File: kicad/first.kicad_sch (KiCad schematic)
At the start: 84 parts, among them J1 Conn_01x04_Pin, P1 USB_C_Plug_USB2.0, Q1 MMUN2111LT1G, Q2 MMBT3904, SW1 SW_SPDT, U1 STM32F407VETx, U2 LP5907MFX-3.3, U3 CS4272, U4 NE5532, U5 NE5532, U6 NE5532, U7 NE5532, Y1 X MHz

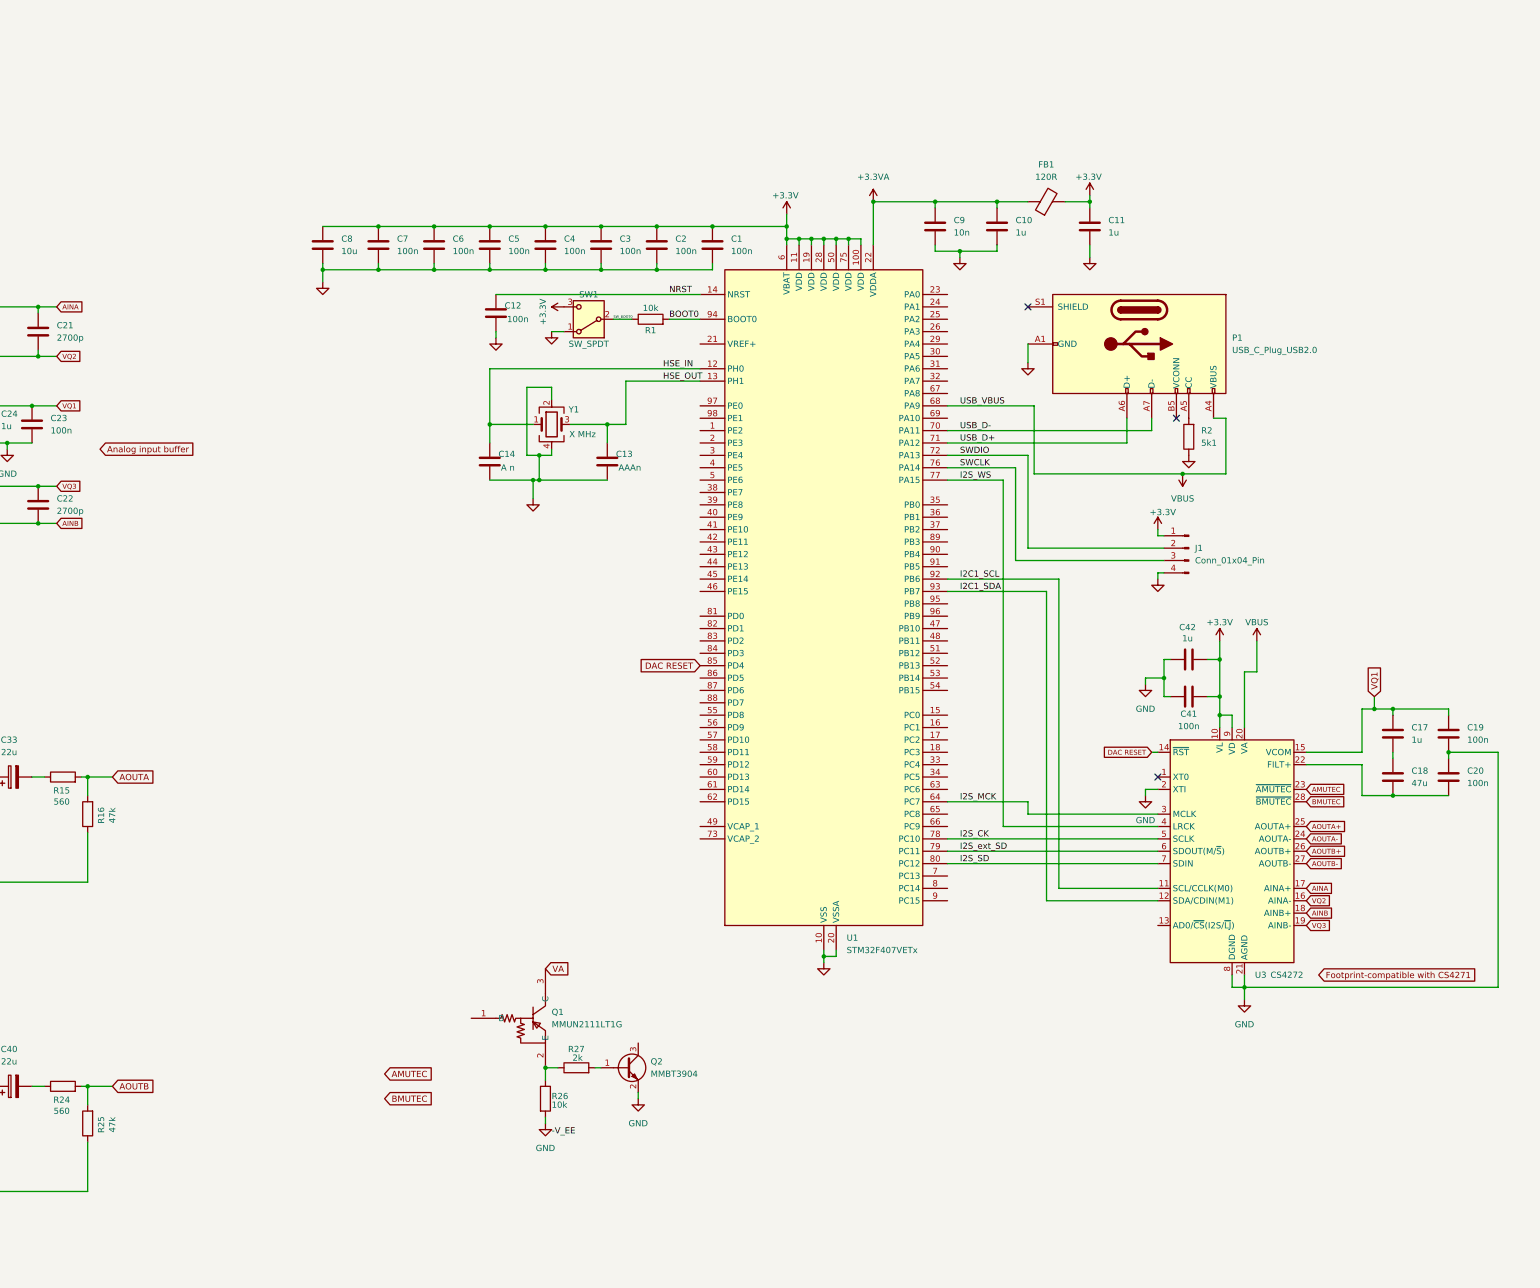
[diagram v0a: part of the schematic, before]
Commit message: codec analog supply filter, added mute control circuits
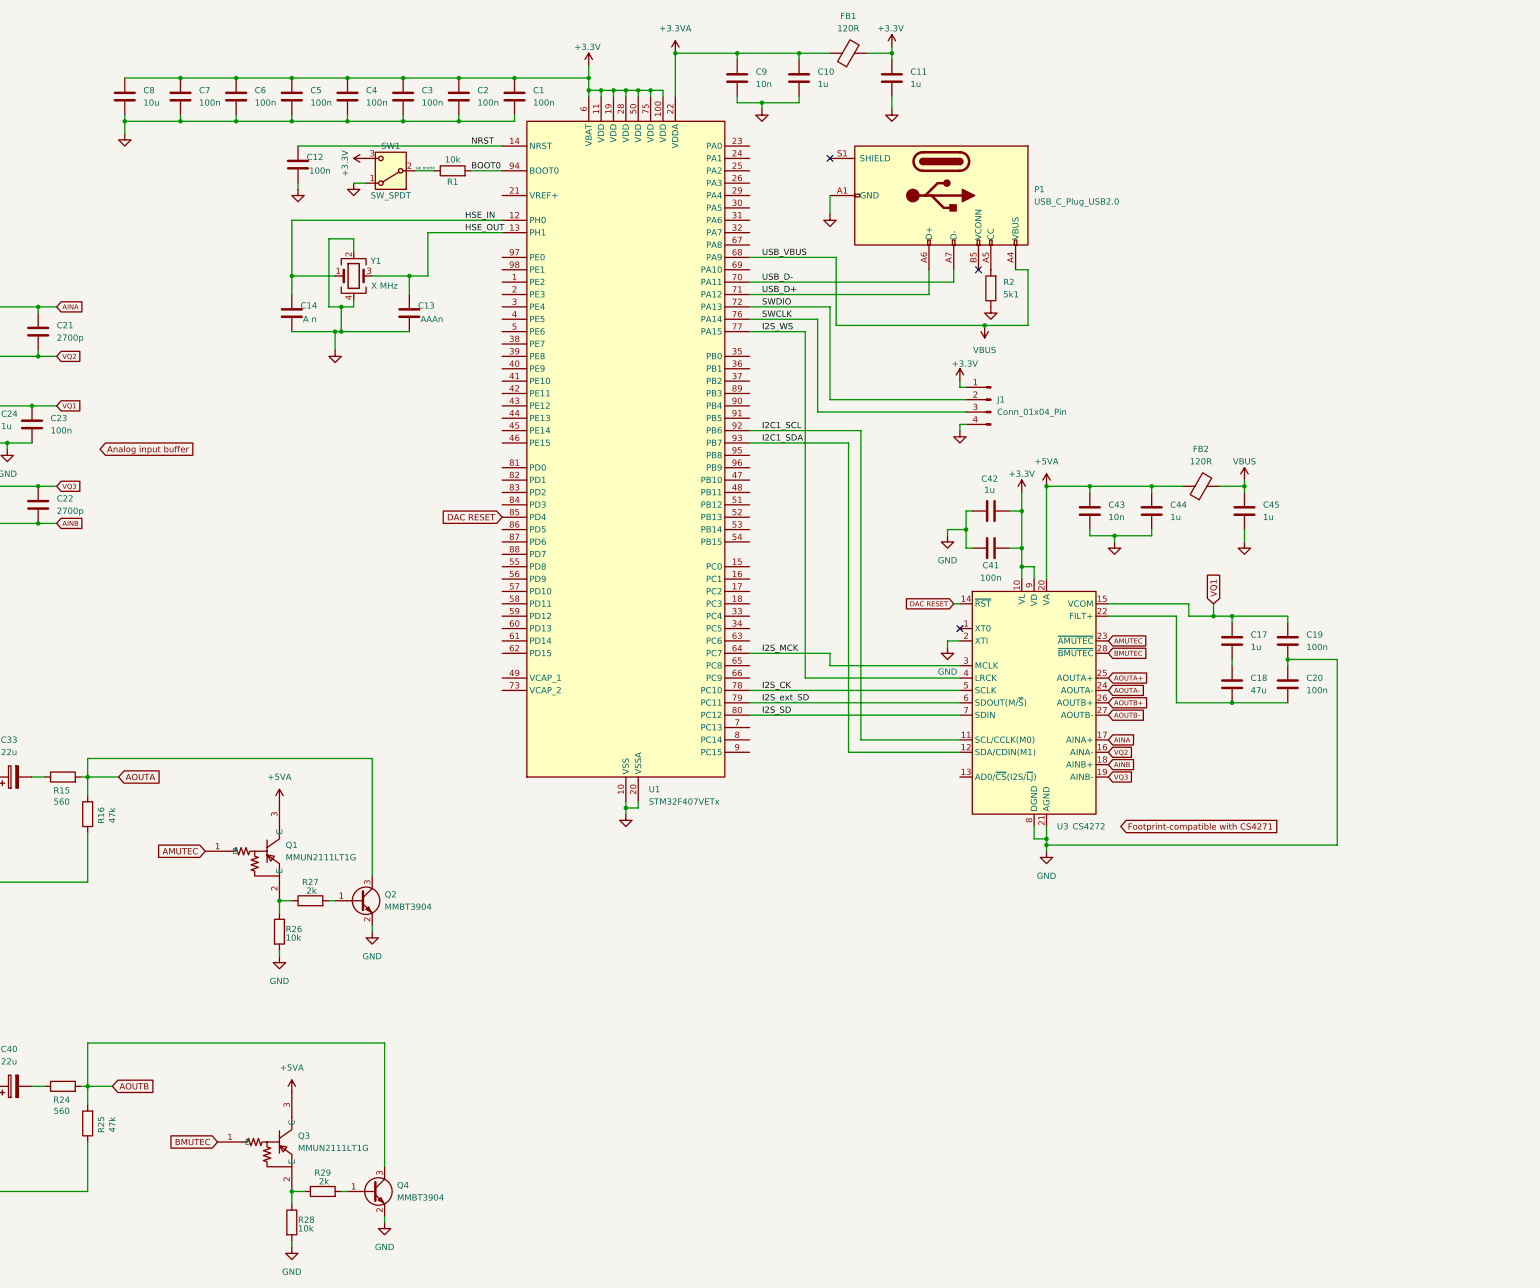
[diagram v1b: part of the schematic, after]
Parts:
- added C43: 10n, symbol Device:C
- added C44, C45: 1u, symbol Device:C
- added FB2: 120R, symbol Device:FerriteBead
- added Q3: MMUN2111LT1G, easyeda2kicad:SOT-23-3_L2.9-W1.3-P1.90-LS2.4-BR, symbol easyeda2kicad:MMUN2111LT1G
- added Q4: MMBT3904, Package_TO_SOT_SMD:SOT-23, symbol Transistor_BJT:MMBT3904
- added R28: 10k, symbol Device:R
- added R29: 2k, symbol Device:R
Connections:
- net AMUTEC: now also Q1.1 (B)
- net AOUTA: now also Q2.3 (C)
- net AOUTB: now also Q4.3 (C)
- net BMUTEC: now also Q3.1 (B)
- net GND: now also C43.2, C44.2, C45.2, Q4.2 (E), R28.2
- net VBUS: now also C45.1, FB2.2; no longer U3.20 (VA)
- net VA renamed +5VA
- net +5VA: now also U3.20 (VA), C43.1, C44.1, FB2.1, Q3.3 (C)
- new net: Q3.2 (E), R28.1, R29.1
- new net: Q4.1 (B), R29.2
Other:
- moved on the sheet: C1, C10, C11, C12, C13, C14, C17, C18, C19, C2, C20, C3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

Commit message: descriptive text
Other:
- note added: "Analog input buffer"
- note added: "Analog output filters"
- note added: "Debug connector"
- note added: "Footprint compatible with CS4271"
- note added: "Mute circuits"
- moved on the sheet: C15, C16, D1, R3, U2

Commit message: rotary encoders
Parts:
- added SW2, SW3, SW4: RotaryEncoder_Switch_MP, symbol Device:RotaryEncoder_Switch_MP
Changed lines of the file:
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@@
 	)
 	(symbol
+		(lib_id "Device:RotaryEncoder_Switch_MP")
+		(at 275.59 214.63 0)
+		(unit 1)
+		(exclude_from_sim no)
+		(in_bom yes)
+		(on_board yes)
+		(dnp no)
+		(fields_autoplaced yes)
+		(property "Reference" "SW3"
+			(at 275.59 204.47 0)
+			(effects
+				(font
+					(size 1.27 1.27)
+				)
+			)
+		)
+		(property "Value" "RotaryEncoder_Switch_MP"
+			(at 275.59 207.01 0)
+			(effects
+				(font
+					(size 1.27 1.27)
+				)
+			)
+		)
+		(property "Footprint" ""
+			(at 271.78 210.566 0)
+			(effects
+				(font
+					(size 1.27 1.27)
+				)
+				(hide yes)
+			)
+		)
+		(property "Datasheet" "~"
+			(at 275.59 227.33 0)
+			(effects
+				(font
+					(size 1.27 1.27)
+				)
+				(hide yes)
+			)
+		)
+		(property "Description" "Rotary encoder, dual channel, incremental quadrate outputs, with switch and MP Pin"
+			(at 275.59 229.87 0)
+			(effects
+				(font
+					(size 1.27 1.27)
+				)
+				(hide yes)
+			)
+		)
+		(pin "A"
+		)
+		(pin "MP"
+		)
+		(pin "S1"
+		)
+		(pin "C"
+		)
+		(pin "B"
+		)
+		(pin "S2"
+		)
+		(instances
+			(project "first"
+				(path "/580becc7-fa47-4b4d-a43e-4b9316967eb7"
+					(reference "SW3")
+					(unit 1)
+				)
+			)
+		)
+	)
+	(symbol
 		(lib_id "Device:R")
 		(at 373.38 35.56 0)
@@
 	)
 	(symbol
+		(lib_id "Device:RotaryEncoder_Switch_MP")
+		(at 246.38 214.63 0)
+		(unit 1)
+		(exclude_from_sim no)
+		(in_bom yes)
+		(on_board yes)
+		(dnp no)
+		(fields_autoplaced yes)
+		(property "Reference" "SW2"
+			(at 246.38 204.47 0)
+			(effects
+				(font
+					(size 1.27 1.27)
+				)
+			)
+		)
+		(property "Value" "RotaryEncoder_Switch_MP"
+			(at 246.38 207.01 0)
+			(effects
+				(font
+					(size 1.27 1.27)
+				)
+			)
+		)
+		(property "Footprint" ""
+			(at 242.57 210.566 0)
+			(effects
+				(font
+					(size 1.27 1.27)
+				)
+				(hide yes)
+			)
+		)
+		(property "Datasheet" "~"
+			(at 246.38 227.33 0)
+			(effects
+				(font
+					(size 1.27 1.27)
+				)
+				(hide yes)
+			)
+		)
+		(property "Description" "Rotary encoder, dual channel, incremental quadrate outputs, with switch and MP Pin"
+			(at 246.38 229.87 0)
+			(effects
+				(font
+					(size 1.27 1.27)
+				)
+				(hide yes)
+			)
+		)
+		(pin "A"
+		)
+		(pin "MP"
+		)
+		(pin "S1"
+		)
+		(pin "C"
+		)
+		(pin "B"
+		)
+		(pin "S2"
+		)
+		(instances
+			(project ""
+				(path "/580becc7-fa47-4b4d-a43e-4b9316967eb7"
+					(reference "SW2")
+					(unit 1)
+				)
+			)
+		)
+	)
+	(symbol
 		(lib_id "Audio:CS4272")
 		(at 311.15 161.29 0)
@@
 					(unit 1)
 				)
+			)
+		)
+	)
+	(symbol
+		(lib_id "Device:RotaryEncoder_Switch_MP")
+		(at 259.08 240.03 0)
+		(unit 1)
+		(exclude_from_sim no)
+		(in_bom yes)
+		(on_board yes)
+		(dnp no)
+		(fields_autoplaced yes)
+		(property "Reference" "SW4"
+			(at 259.08 229.87 0)
+			(effects
+				(font
+					(size 1.27 1.27)
+				)
+			)
+		)
+		(property "Value" "RotaryEncoder_Switch_MP"
+			(at 259.08 232.41 0)
+			(effects
+				(font
+					(size 1.27 1.27)
+				)
+			)
+		)
+		(property "Footprint" ""
+			(at 255.27 235.966 0)
+			(effects
+				(font
+					(size 1.27 1.27)
+				)
+				(hide yes)
+			)
+		)
+		(property "Datasheet" "~"
+			(at 259.08 252.73 0)
+			(effects
+				(font
+					(size 1.27 1.27)
+				)
+				(hide yes)
+			)
+		)
+		(property "Description" "Rotary encoder, dual channel, incremental quadrate outputs, with switch and MP Pin"
+			(at 259.08 255.27 0)
+			(effects
+				(font
+					(size 1.27 1.27)
+				)
+				(hide yes)
+			)
+		)
+		(pin "A"
+		)
+		(pin "MP"
+		)
+		(pin "S1"
+		)
+		(pin "C"
+		)
+		(pin "B"
+		)
+		(pin "S2"
+		)
+		(instances
+			(project "first"
+				(path "/580becc7-fa47-4b4d-a43e-4b9316967eb7"
+					(reference "SW4")
+					(unit 1)
+				)

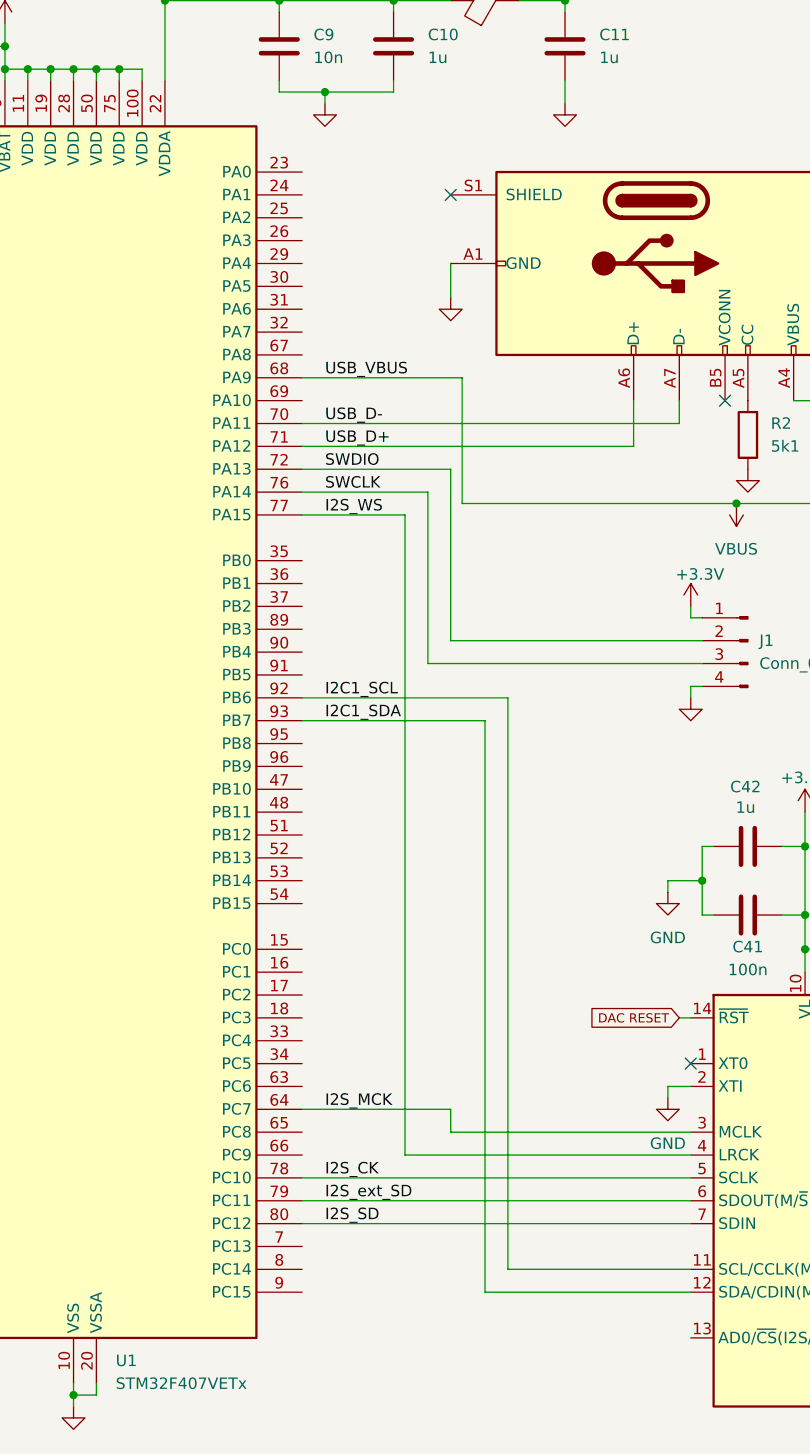
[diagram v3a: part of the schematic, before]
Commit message: assigned timer pins, moved I2C clk and data
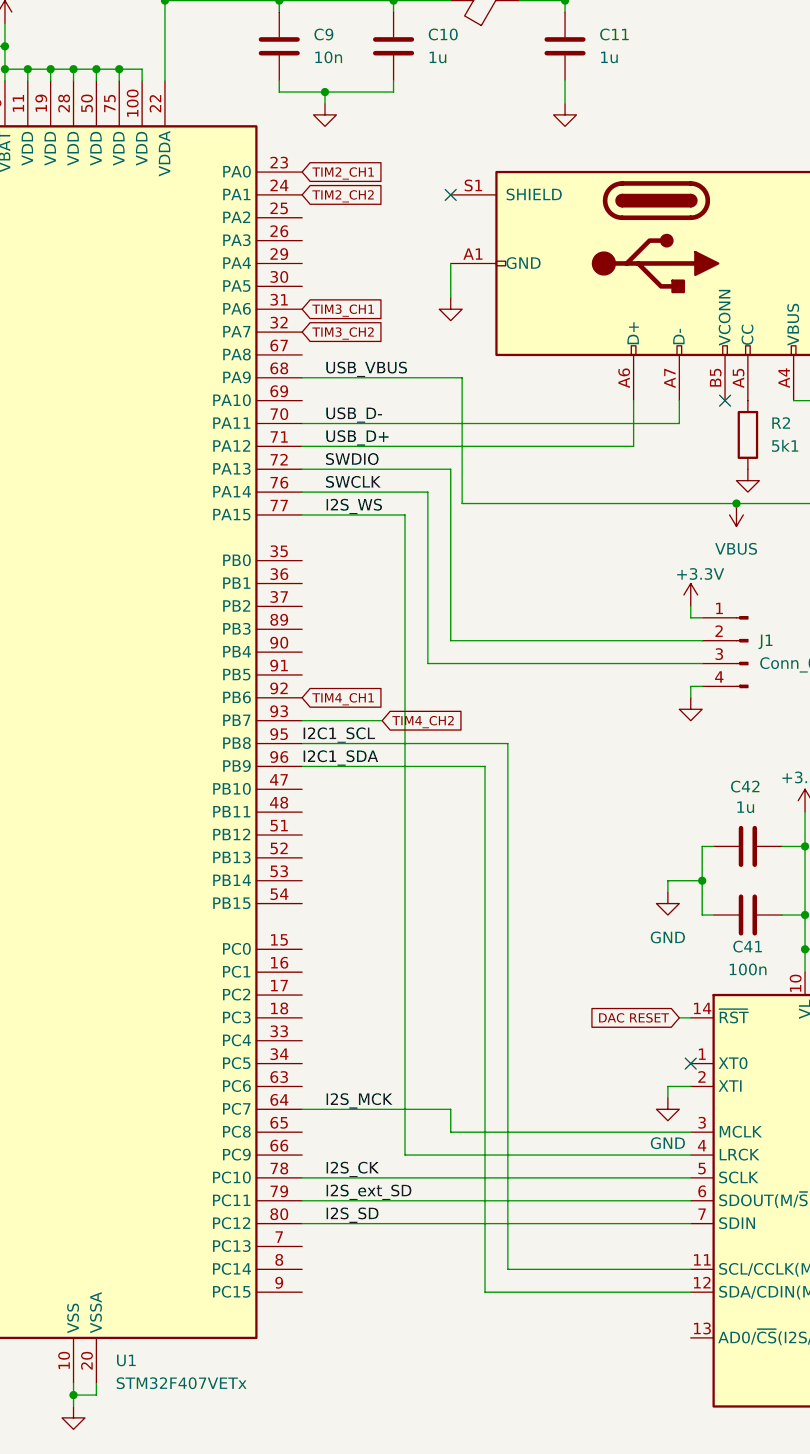
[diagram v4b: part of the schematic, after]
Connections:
- net I2C1_SCL: now also U1.95 (PB8); no longer U1.92 (PB6)
- net I2C1_SDA: now also U1.96 (PB9); no longer U1.93 (PB7)
- net TIM2_CH1: now reaches U1.23 (PA0)
- net TIM2_CH2: now reaches U1.24 (PA1)
- net TIM3_CH1: now reaches U1.31 (PA6)
- net TIM3_CH2: now reaches U1.32 (PA7)
- new net TIM4_CH1: U1.92 (PB6)
- new net TIM4_CH2: U1.93 (PB7)
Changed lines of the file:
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@@
 	(wire
 		(pts
-			(xy 59.69 123.19) (xy 59.69 115.57)
+			(xy 252.73 113.03) (xy 273.05 113.03)
 		)
 		(stroke
@@
 	(wire
 		(pts
-			(xy 252.73 107.95) (xy 273.05 107.95)
+			(xy 59.69 123.19) (xy 59.69 115.57)
 		)
 		(stroke
@@
 	(wire
 		(pts
-			(xy 275.59 105.41) (xy 275.59 168.91)
+			(xy 322.58 118.11) (xy 322.58 116.84)
 		)
 		(stroke
@@
 	(wire
 		(pts
-			(xy 322.58 118.11) (xy 322.58 116.84)
+			(xy 347.98 140.97) (xy 347.98 143.51)
 		)
 		(stroke
@@
 	(wire
 		(pts
-			(xy 347.98 140.97) (xy 347.98 143.51)
+			(xy 76.2 237.49) (xy 78.74 237.49)
 		)
 		(stroke
@@
 	(wire
 		(pts
-			(xy 76.2 237.49) (xy 78.74 237.49)
+			(xy 168.91 261.62) (xy 170.18 261.62)
 		)
 		(stroke
@@
 	(wire
 		(pts
-			(xy 168.91 261.62) (xy 170.18 261.62)
+			(xy 307.34 72.39) (xy 309.88 72.39)
 		)
 		(stroke
@@
 	(wire
 		(pts
-			(xy 307.34 72.39) (xy 309.88 72.39)
+			(xy 275.59 110.49) (xy 275.59 168.91)
 		)
 		(stroke
@@
 	(wire
 		(pts
-			(xy 273.05 107.95) (xy 273.05 171.45)
-		)
-		(stroke
-			(width 0)
-			(type default)
-		)
-	)
-	(wire
-		(pts
 			(xy 373.38 39.37) (xy 373.38 41.91)
 		)
@@
 	(wire
 		(pts
+			(xy 273.05 113.03) (xy 273.05 171.45)
+		)
+		(stroke
+			(width 0)
+			(type default)
+		)
+	)
+	(wire
+		(pts
 			(xy 110.49 80.01) (xy 106.68 80.01)
 		)
@@
 	(wire
 		(pts
-			(xy 252.73 105.41) (xy 275.59 105.41)
-		)
-		(stroke
-			(width 0)
-			(type default)
-		)
-	)
-	(wire
-		(pts
 			(xy 175.26 73.66) (xy 182.88 73.66)
 		)
@@
 	(wire
 		(pts
+			(xy 252.73 110.49) (xy 275.59 110.49)
+		)
+		(stroke
+			(width 0)
+			(type default)
+		)
+	)
+	(wire
+		(pts
 			(xy 39.37 265.43) (xy 39.37 261.62)
 		)
@@
 	(wire
 		(pts
+			(xy 261.62 107.95) (xy 252.73 107.95)
+		)
+		(stroke
+			(width 0)
+			(type default)
+		)
+	)
+	(wire
+		(pts
 			(xy 166.37 80.01) (xy 168.91 80.01)
 		)
@@
 	)
 	(label "I2C1_SDA"
-		(at 255.27 107.95 0)
+		(at 252.73 113.03 0)
 		(effects
 			(font
@@
 	)
 	(label "I2C1_SCL"
-		(at 255.27 105.41 0)
+		(at 252.73 110.49 0)
 		(effects
 			(font
@@
 		)
 	)
+	(global_label "TIM2_CH2"
+		(shape input)
+		(at 252.73 49.53 0)
+		(fields_autoplaced yes)
+		(effects
+			(font
+				(size 1.016 1.016)
+			)
+			(justify left)
+		)
+		(property "Intersheetrefs" "${INTERSHEET_REFS}"
+			(at 262.3266 49.53 0)
+			(effects
+				(font
+					(size 1.27 1.27)
+				)
+				(justify left)
+				(hide yes)
+			)
+		)
+	)
 	(global_label "AOUTA+"
 		(shape input)
@@
 		)
 	)
+	(global_label "TIM4_CH1"
+		(shape input)
+		(at 252.73 105.41 0)
+		(fields_autoplaced yes)
+		(effects
+			(font
+				(size 1.016 1.016)
+			)
+			(justify left)
+		)
+		(property "Intersheetrefs" "${INTERSHEET_REFS}"
+			(at 262.3266 105.41 0)
+			(effects
+				(font
+					(size 1.27 1.27)
+				)
+				(justify left)
+				(hide yes)
+			)
+		)
+	)
 	(global_label "AINR"
 		(shape input)
@@
 		)
 	)
+	(global_label "TIM2_CH1"
+		(shape input)
+		(at 252.73 46.99 0)
+		(fields_autoplaced yes)
+		(effects
+			(font
+				(size 1.016 1.016)
+			)
+			(justify left)
+		)
+		(property "Intersheetrefs" "${INTERSHEET_REFS}"
+			(at 262.3266 46.99 0)
+			(effects
+				(font
+					(size 1.27 1.27)
+				)
+				(justify left)
+				(hide yes)
+			)
+		)
+	)
+	(global_label "TIM4_CH2"
+		(shape input)
+		(at 261.62 107.95 0)
+		(fields_autoplaced yes)
+		(effects
+			(font
+				(size 1.016 1.016)
+			)
+			(justify left)
+		)
+		(property "Intersheetrefs" "${INTERSHEET_REFS}"
+			(at 271.2166 107.95 0)
+			(effects
+				(font
+					(size 1.27 1.27)
+				)
+				(justify left)
+				(hide yes)
+			)
+		)
+	)
 	(global_label "AOUTA+"
 		(shape input)
@@
 				(hide yes)
 			)
+		)
+	)
+	(global_label "TIM3_CH2"
+		(shape input)
+		(at 252.73 64.77 0)
+		(fields_autoplaced yes)
+		(effects
+			(font
+				(size 1.016 1.016)
+			)
+			(justify left)
+		)
+		(property "Intersheetrefs" "${INTERSHEET_REFS}"
+			(at 262.3266 64.77 0)
+			(effects
+				(font
+					(size 1.27 1.27)
+				)
+				(justify left)
+				(hide yes)
+			)
+		)
+	)
+	(global_label "TIM3_CH1"
+		(shape input)
+		(at 252.73 62.23 0)
+		(fields_autoplaced yes)
+		(effects
+			(font
+				(size 1.016 1.016)
+			)
+			(justify left)
+		)
+		(property "Intersheetrefs" "${INTERSHEET_REFS}"
+			(at 262.3266 62.23 0)
+			(effects
+				(font
+					(size 1.27 1.27)
+				)
+				(justify left)
+				(hide yes)
+			)
